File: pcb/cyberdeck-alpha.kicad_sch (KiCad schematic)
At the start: 516 parts, among them J1 CPU_FAN, J10 Conn_01x30, J11 Conn_01x22, J12 HDMI_C_1.3, J13 USB_C_Receptacle_USB2.0_16P, J14 Conn_01x06, J15 Conn_02x20_Odd_Even, J16 1-2199119-5, J17 2199119-3, J18 SIM_Card, J19 TSOP77438TR, J2 GP_LB, J20 Conn_01x22, J21 DX07S024JJ2R1300, J22 USB3_A, J3 GP_RB, J4 JOYSTICK, J5 Conn_01x06_Pin, J6 USB_C_Receptacle_USB2.0_16P, J7 Conn_01x05, J8 PJ-342B, J9 SPK, Q1 IRLML6244, Q2 CJ2101, Q3 SI4174DY-T1-GE3_N-Channel_FET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, Q4 BSS138, Q5 IRLML6244, Q6 SI4174DY-T1-GE3_N-Channel_FET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, Q7 SI4174DY-T1-GE3_N-Channel_FET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, Q8 SI4174DY-T1-GE3_N-Channel_FET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, U1 W25Q128JVS, U10 TPS62180YZFR, U11 TPS62180YZFR, U12 SY6280_OCP, U13 FAN5333ASX, U14 USBLC6-2SC6, U15 SY6280_OCP, U16 BQ76905RGRR, U17 ATtiny202-SS, U18 TPS25751SRSMR, U19 HD3SS3220IRNHT, U2 STM32F072CBT6, U20 TPD4EUSB30DQAR, U21 TPD4EUSB30DQAR, U22 AT24CS01-SSHM, U3 XC6206, U4 BQ25792RQMR, U5 RP2040, U6 USBLC6-2SC6, U7 CH334R, U8 PAM8406AB, U9 PCM2706CPJT, X1 X322512MSB4SI, X2 X322512MSB4SI, X3 X322512MSB4SI

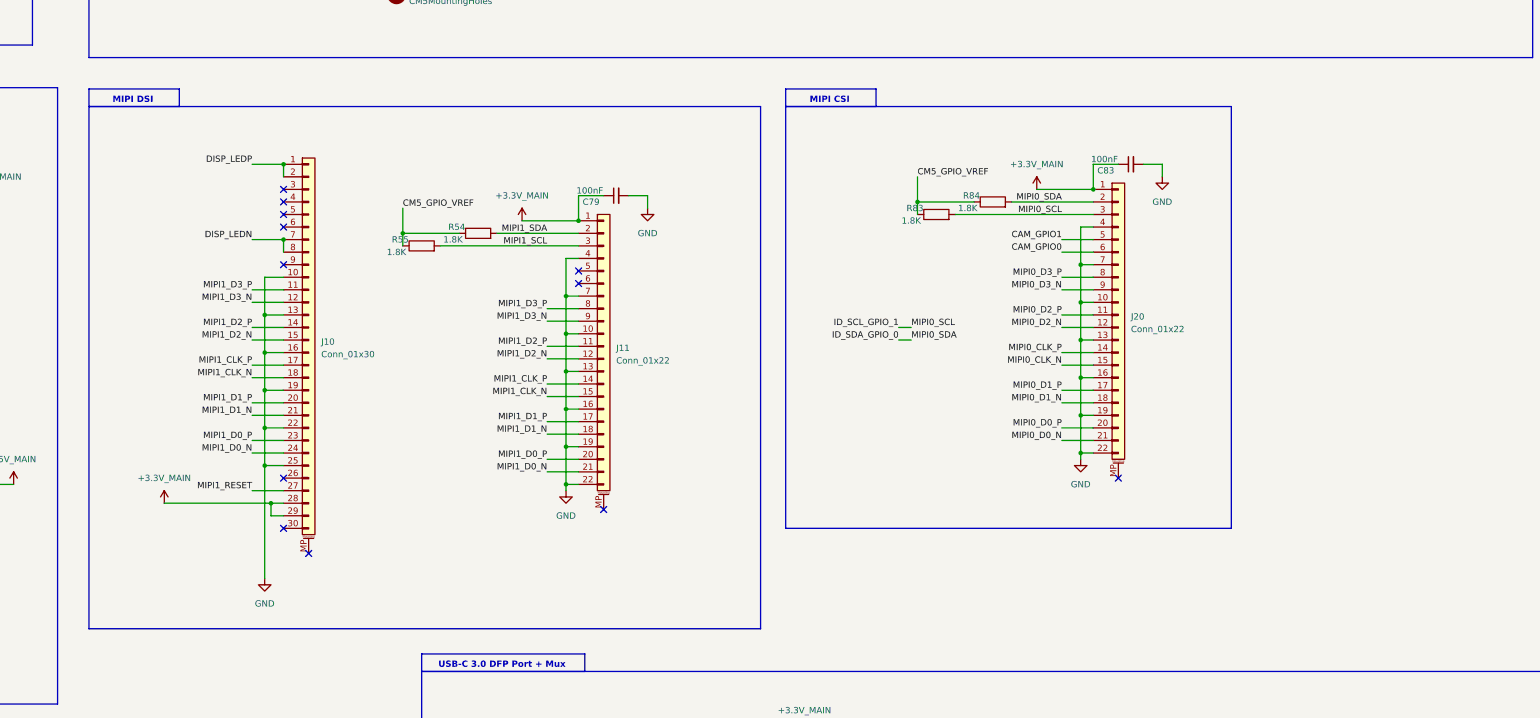
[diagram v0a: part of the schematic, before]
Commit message: add solder jumpers to MIPI DSI and length match traces
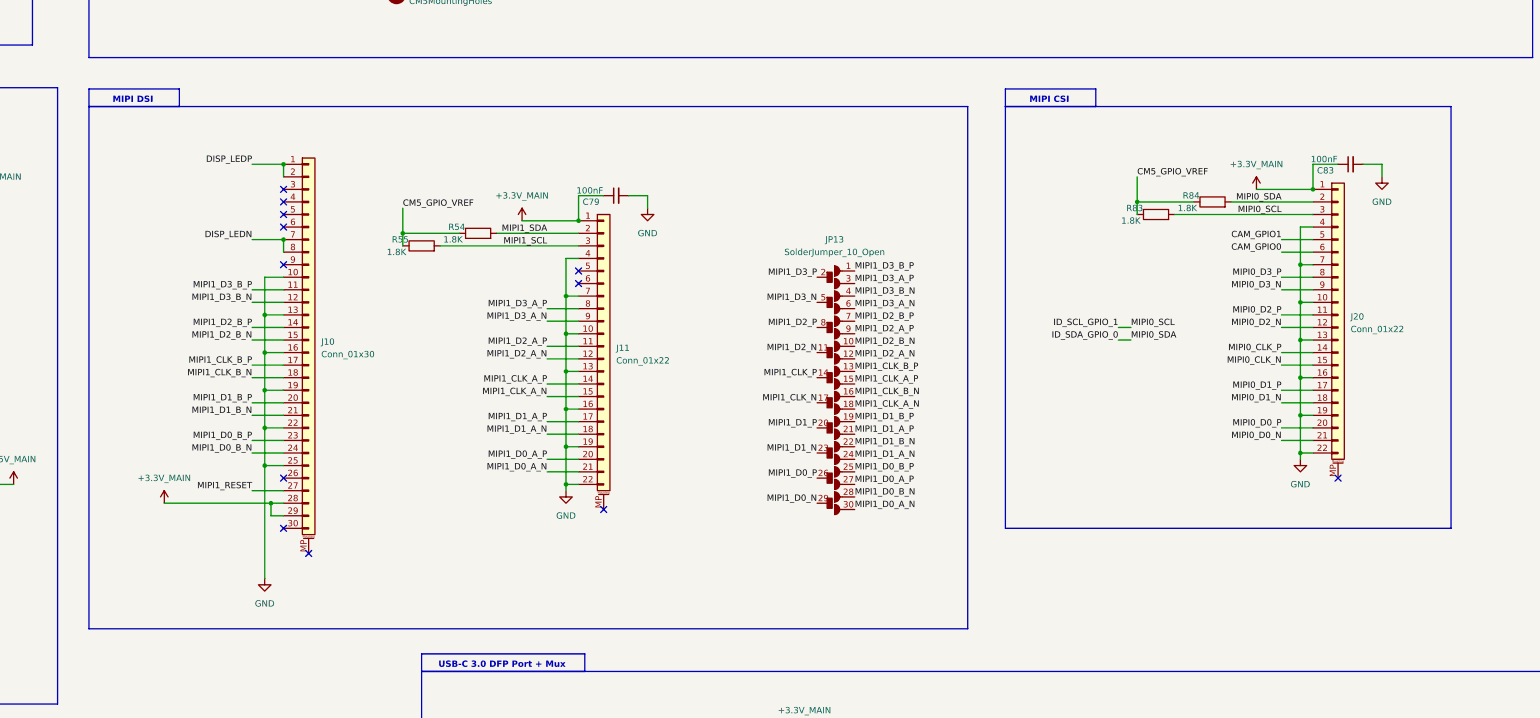
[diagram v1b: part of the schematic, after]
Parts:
- added JP13: SolderJumper_10_Open, LibraryGlobalFootprints:SolderJumper-10, symbol LibraryGlobalSymbols:SolderJumper_10_Open
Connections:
- net MIPI1_CLK_N: now also JP13.17; no longer J10.18 (Pin_18), J11.15 (Pin_15)
- net MIPI1_CLK_P: now also JP13.14; no longer J10.17 (Pin_17), J11.14 (Pin_14)
- net MIPI1_D0_N: now also JP13.29; no longer J10.24 (Pin_24), J11.21 (Pin_21)
- net MIPI1_D0_P: now also JP13.26; no longer J10.23 (Pin_23), J11.20 (Pin_20)
- net MIPI1_D1_N: now also JP13.23; no longer J10.21 (Pin_21), J11.18 (Pin_18)
- net MIPI1_D1_P: now also JP13.20; no longer J10.20 (Pin_20), J11.17 (Pin_17)
- net MIPI1_D2_N: now also JP13.11; no longer J10.15 (Pin_15), J11.12 (Pin_12)
- net MIPI1_D2_P: now also JP13.8; no longer J10.14 (Pin_14), J11.11 (Pin_11)
- net MIPI1_D3_N: now also JP13.5; no longer J10.12 (Pin_12), J11.9 (Pin_9)
- net MIPI1_D3_P: now also JP13.2; no longer J10.11 (Pin_11), J11.8 (Pin_8)
- new net MIPI1_CLK_A_N: J11.15 (Pin_15), JP13.18
- new net MIPI1_CLK_A_P: J11.14 (Pin_14), JP13.15
- new net MIPI1_CLK_B_N: J10.18 (Pin_18), JP13.16
- new net MIPI1_CLK_B_P: J10.17 (Pin_17), JP13.13
- new net MIPI1_D0_A_N: J11.21 (Pin_21), JP13.30
- new net MIPI1_D0_A_P: J11.20 (Pin_20), JP13.27
- new net MIPI1_D0_B_N: J10.24 (Pin_24), JP13.28
- new net MIPI1_D0_B_P: J10.23 (Pin_23), JP13.25
- new net MIPI1_D1_A_N: J11.18 (Pin_18), JP13.24
- new net MIPI1_D1_A_P: J11.17 (Pin_17), JP13.21
- new net MIPI1_D1_B_N: J10.21 (Pin_21), JP13.22
- new net MIPI1_D1_B_P: J10.20 (Pin_20), JP13.19
- new net MIPI1_D2_A_N: J11.12 (Pin_12), JP13.12
- new net MIPI1_D2_A_P: J11.11 (Pin_11), JP13.9
- new net MIPI1_D2_B_N: J10.15 (Pin_15), JP13.10
- new net MIPI1_D2_B_P: J10.14 (Pin_14), JP13.7
- new net MIPI1_D3_A_N: J11.9 (Pin_9), JP13.6
- new net MIPI1_D3_A_P: J11.8 (Pin_8), JP13.3
- new net MIPI1_D3_B_N: J10.12 (Pin_12), JP13.4
- new net MIPI1_D3_B_P: J10.11 (Pin_11), JP13.1
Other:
- moved on the sheet: C83, J20, R83, R84

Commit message: added solder jumpers for DSI and USB source (CM4 compatibility)
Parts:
- added C124: 10uF, Capacitor_SMD:C_0603_1608Metric, symbol Device:C_Small
- added C125: 100nF, Capacitor_SMD:C_0402_1005Metric, symbol Device:C_Small
- added C126: 22uF, Capacitor_SMD:C_0805_2012Metric, symbol Device:C
- added R65: 0R, Resistor_SMD:R_0402_1005Metric, symbol Device:R
- added U23: CH334R, Package_SO:QSOP-16_3.9x4.9mm_P0.635mm, symbol Interface_USB:CH334R
- added X4: X322512MSB4SI, Crystal:Crystal_SMD_3225-4Pin_3.2x2.5mm, symbol Device:Crystal_GND24
- J22: now fitted; now in the parts list
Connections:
- net +5V_HUB: now also R65.2
- net GND: now also C124.2, C125.1, C126.1, U23.14 (GND), X4.2, X4.4
- net HUB_DS_3_D+ renamed HUB2_DS_0_D+
- net HUB2_DS_0_D+: now also U23.8 (DP1+); no longer U7.2 (DP4+)
- net HUB_DS_3_D- renamed HUB2_DS_0_D-
- net HUB2_DS_0_D-: now also U23.7 (DM1-); no longer U7.1 (DM4-)
- new net: C126.2, R65.1, U23.12 (V5)
- new net: C124.1, C125.2, U23.13 (VDD33)
- new net: U23.15 (XO), X4.1
- new net: U23.16 (XI), X4.3
- new net HUB2_DS_1_D+: U23.6 (DP2+)
- new net HUB2_DS_1_D-: U23.5 (DM2-)
- new net HUB2_DS_2_D+: U23.4 (DP3+)
- new net HUB2_DS_2_D-: U23.3 (DM3-)
- new net HUB2_DS_3_D+: U23.2 (DP4+)
- new net HUB2_DS_3_D-: U23.1 (DM4-)
- new net HUB2_US_D+: U23.11 (DPU+), U7.2 (DP4+)
- new net HUB2_US_D-: U23.10 (DMU-), U7.1 (DM4-)
- no-connect marks 114 -> 115
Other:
- note added: "Ilim (A) = 6800 / Rset (ohm) 3.4K = 2A, 6.8K = 1A, 10K = 0.68A"
- note removed: "Ilim (A) = 6800 / Rset (ohm)"
- moved on the sheet: C123, C28, C32, C33, JP1, JP2, R42, SJ1, SJ2, U22, U7, X1

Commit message: fix button part number
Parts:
- K_79: LCSC C7470157 -> C7470150
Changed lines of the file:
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@@
 			)
 		)
-		(property "LCSC" "C7470157"
+		(property "LCSC" "C7470150"
 			(at 121.92 354.33 0)
 			(effects
